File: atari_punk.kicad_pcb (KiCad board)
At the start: 2 copper layers, 50.2 x 41.3 mm, 12 parts, among them J1 Conn_01x02_MountingPin, J2 Conn_01x02_MountingPin, U1 NE555P, U2 NE555P

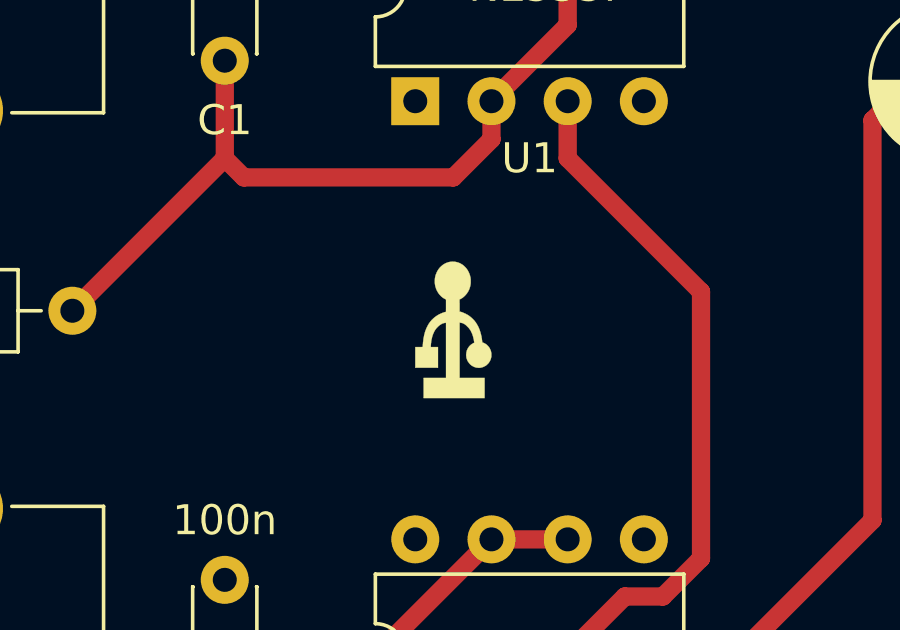
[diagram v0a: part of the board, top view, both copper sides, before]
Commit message: Changed Niubit logo.
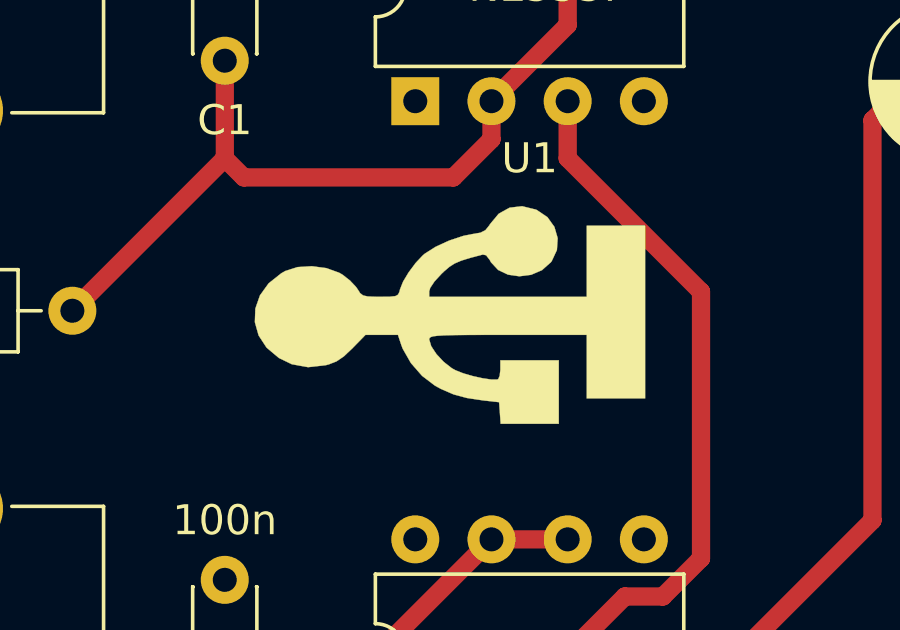
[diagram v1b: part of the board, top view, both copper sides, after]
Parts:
- removed the G*** at (116.2, 120.7)
- added G***: LOGO, eduardofilo_footprints:niubit_logo_13mm, F.Cu at (116.1, 120.1)

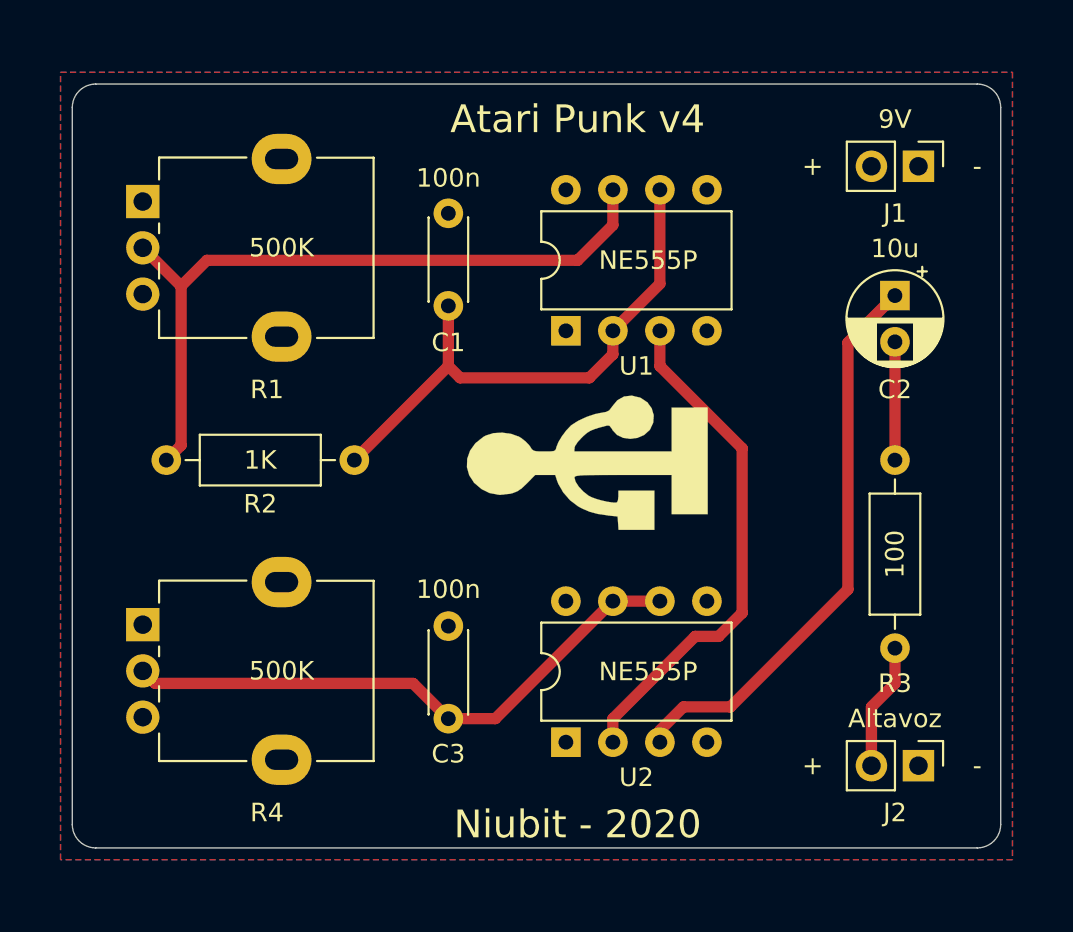
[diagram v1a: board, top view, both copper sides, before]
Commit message: Added resistors. Added big Niubit logo. Added holes for mounting.
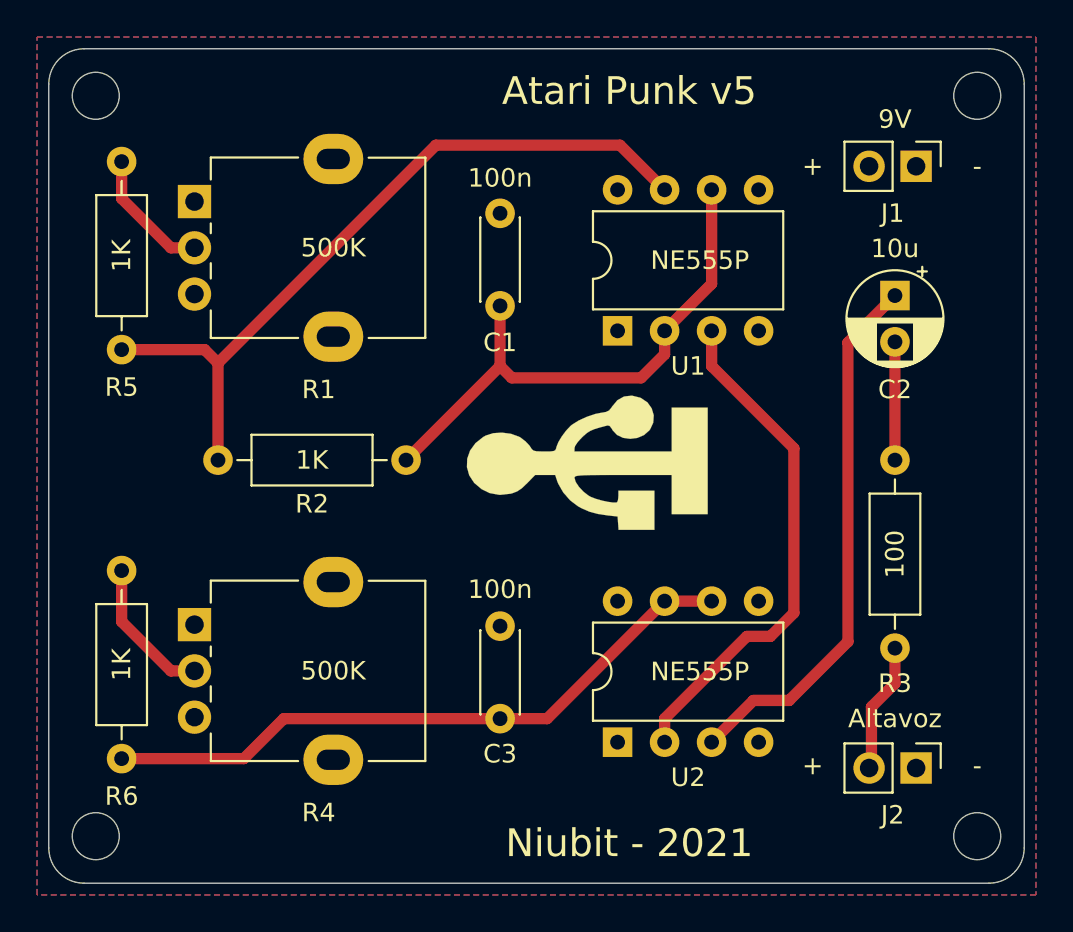
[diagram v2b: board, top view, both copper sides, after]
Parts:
- added G***: LOGO, eduardofilo_footprints:niubit_logo_52mm, B.Cu at (113.3, 120.0)
- added R5: 1K, Resistor_THT:R_Axial_DIN0207_L6.3mm_D2.5mm_P10.16mm_Horizontal, F.Cu at (90.9, 114.0)
- added R6: 1K, Resistor_THT:R_Axial_DIN0207_L6.3mm_D2.5mm_P10.16mm_Horizontal, F.Cu at (90.9, 136.1)
- J1, J2: value Conn_01x02_MountingPin -> Conn_01x02_Male
- moved C1 2.79 mm to (111.4, 106.7)
- moved C3 2.79 mm to (111.4, 134.0)
- moved R2 2.79 mm to (106.3, 120.0)
- moved R1 2.79 mm to (94.9, 106.0)
- moved R4 2.79 mm to (94.9, 128.9)
- moved U1 2.79 mm to (117.7, 113.0)
- moved U2 2.79 mm to (117.7, 135.3)
- moved J2 0.18 mm to (133.9, 136.7)
- moved J1 0.13 mm to (133.9, 104.1)
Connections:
- R2 pad 2: Net-(R1-Pad2) -> Net-(R2-Pad2)
- R4 pad 2: Net-(C3-Pad1) -> Net-(R4-Pad2)
- U1 pad 7: Net-(R1-Pad2) -> Net-(R2-Pad2)
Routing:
- net Net-(R2-Pad2): track 0.00 -> 40.8 mm
- net Net-(R1-Pad2): track 39.3 -> 7.04 mm
- net Net-(R4-Pad2): track 0.00 -> 7.80 mm
- net Net-(C3-Pad1): track 31.6 -> 35.4 mm
- net Net-(C2-Pad1): track 30.9 -> 29.4 mm
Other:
- board size 50.2 x 41.3 mm -> 52.7 x 45.1 mm
- board text added: "Atari Punk v5"
- board text added: "Niubit - 2021"
- board text removed: "Atari Punk v4"
- board text removed: "Niubit - 2020"

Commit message: Se incorpora interruptor de encendido.
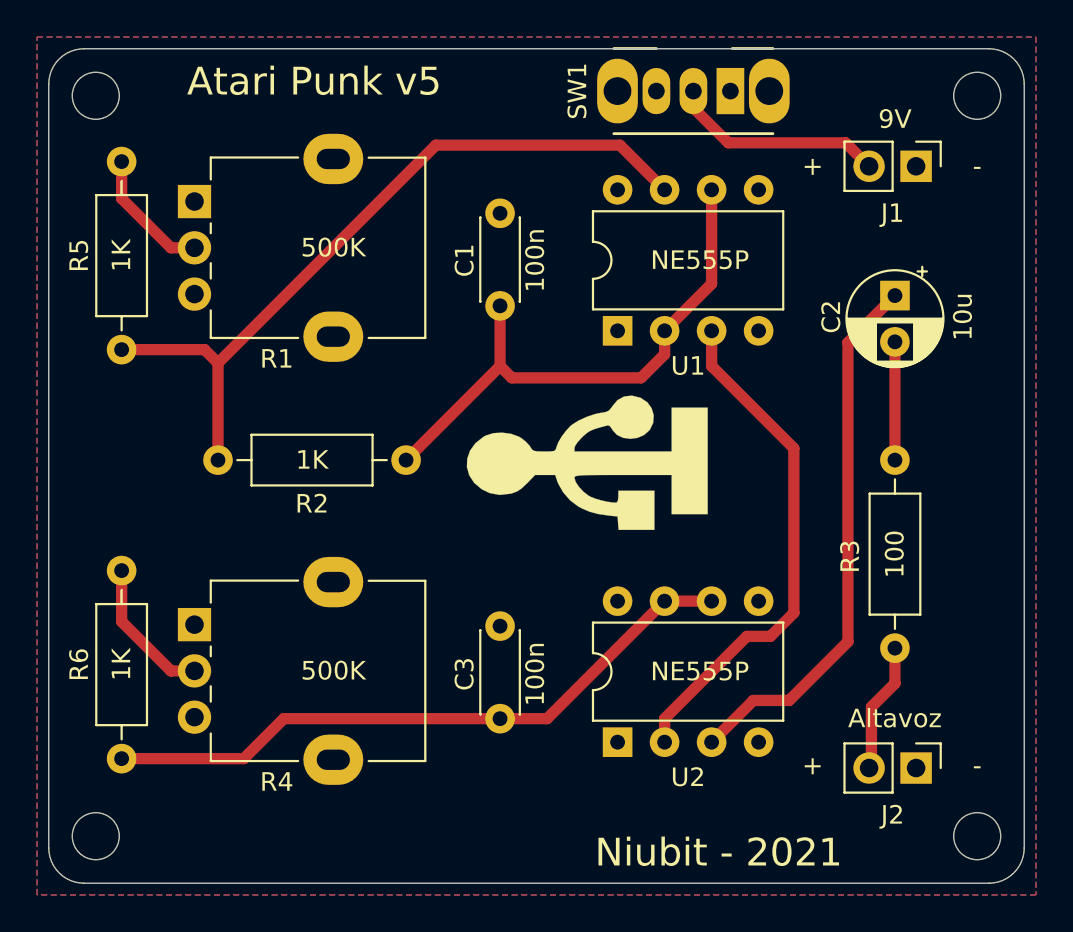
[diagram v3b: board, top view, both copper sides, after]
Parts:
- added SW1: SK12D07VG4, Button_Switch_THT:SW_CuK_OS102011MA1QN1_SPDT_Angled, F.Cu at (123.8, 100.1)
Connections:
- J1 pad 2: +9V -> Net-(J1-Pad2)
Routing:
- net Net-(J1-Pad2): track 0.00 -> 11.7 mm

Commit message: Cambio menor.
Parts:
- moved G*** 3.06 mm to (119.1, 120.4), turned to 270 degrees

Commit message: Logo Niubit en cara inferior de 35mm de altura en lugar de 52mm.
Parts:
- removed the G*** at (113.3, 120.0)
- added G***: LOGO, eduardofilo_footprints:niubit_logo_35mm, B.Cu at (113.4, 120.4)

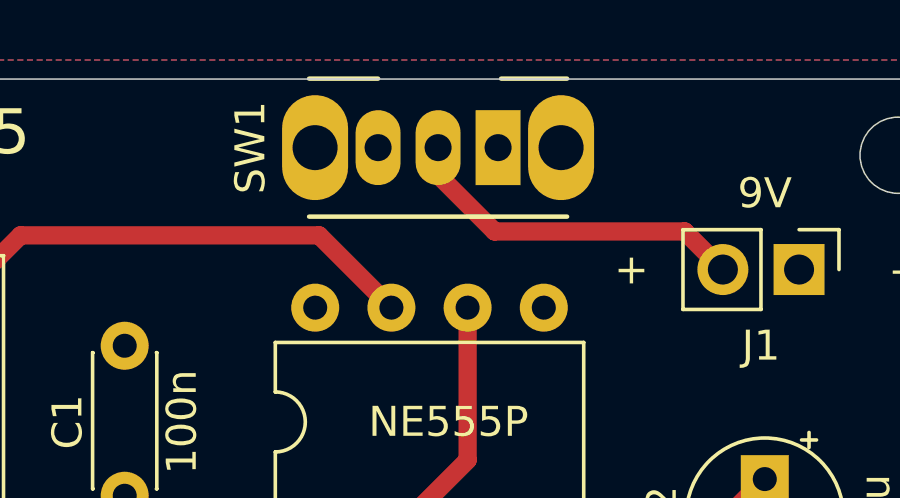
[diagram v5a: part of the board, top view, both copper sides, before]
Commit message: Leyenda ON/OFF.
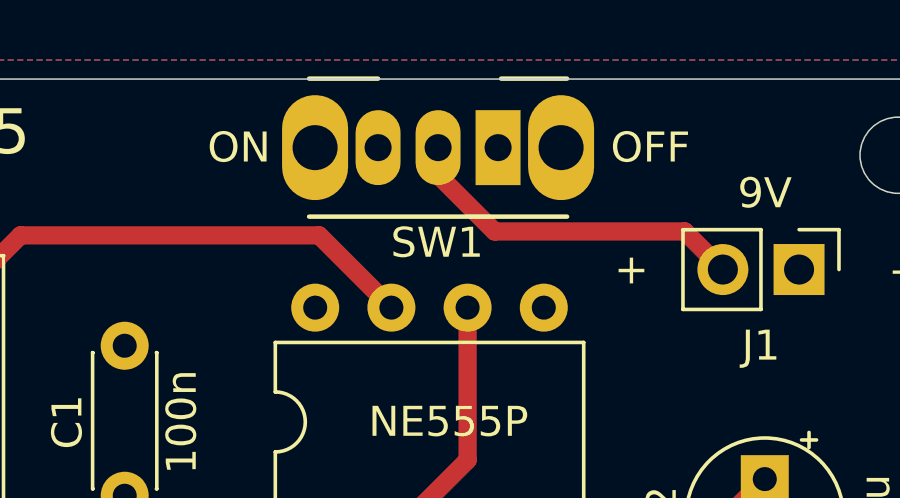
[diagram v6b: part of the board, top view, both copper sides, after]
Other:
- board text added: "OFF"
- board text added: "ON"
